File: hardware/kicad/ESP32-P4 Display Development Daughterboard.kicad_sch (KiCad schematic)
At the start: 0 parts

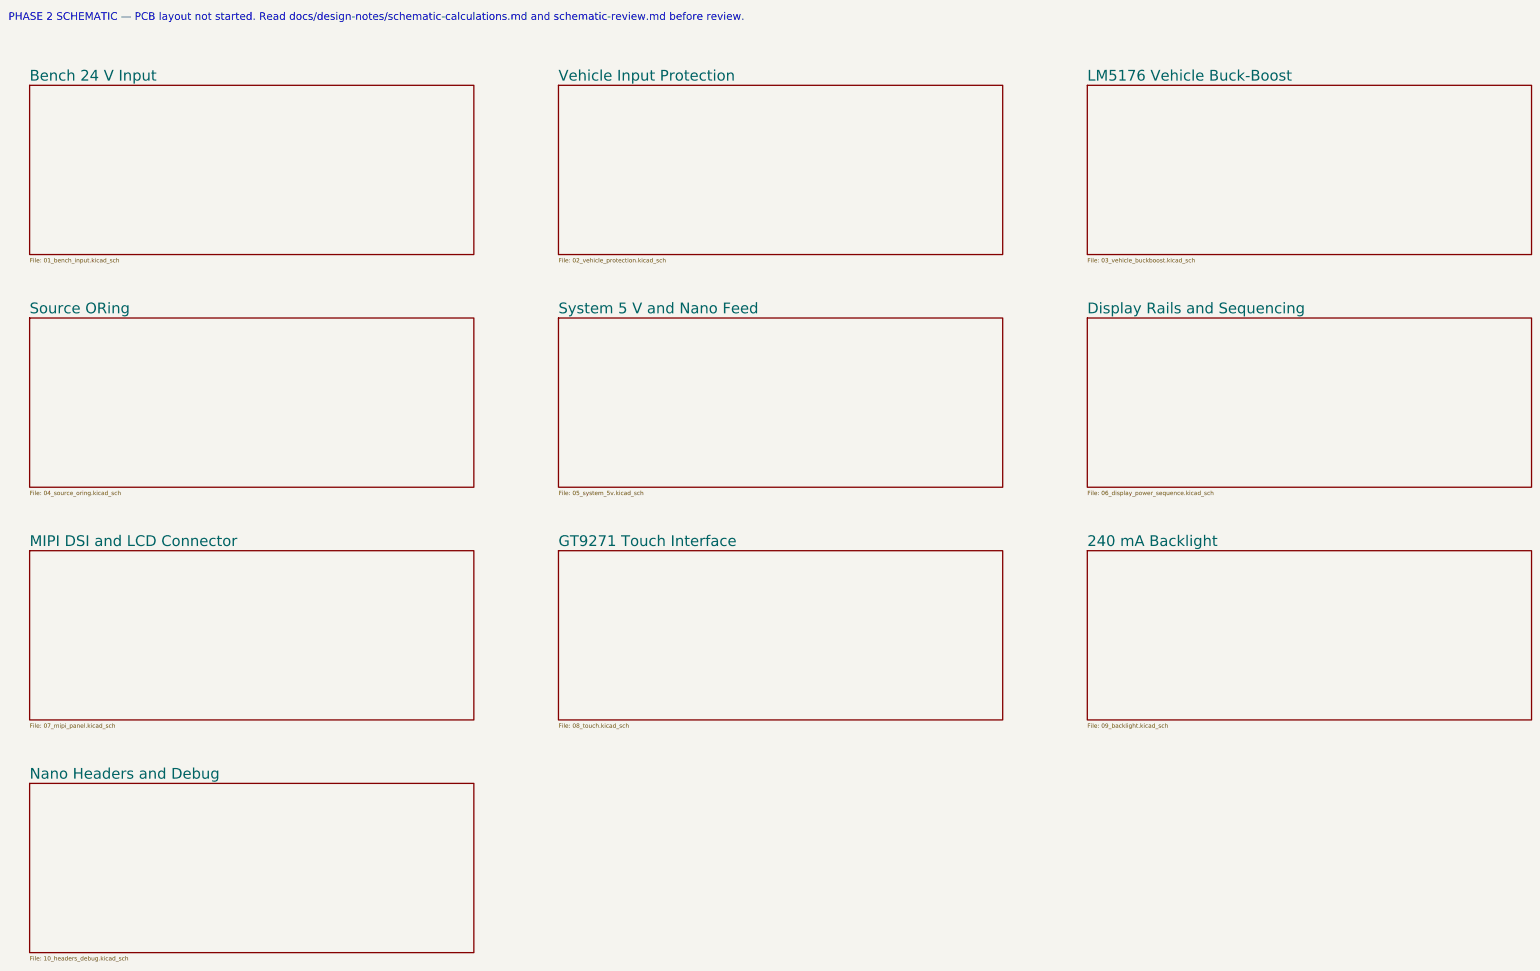
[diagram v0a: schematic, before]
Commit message: hardware: complete schematic maintainability and libraries
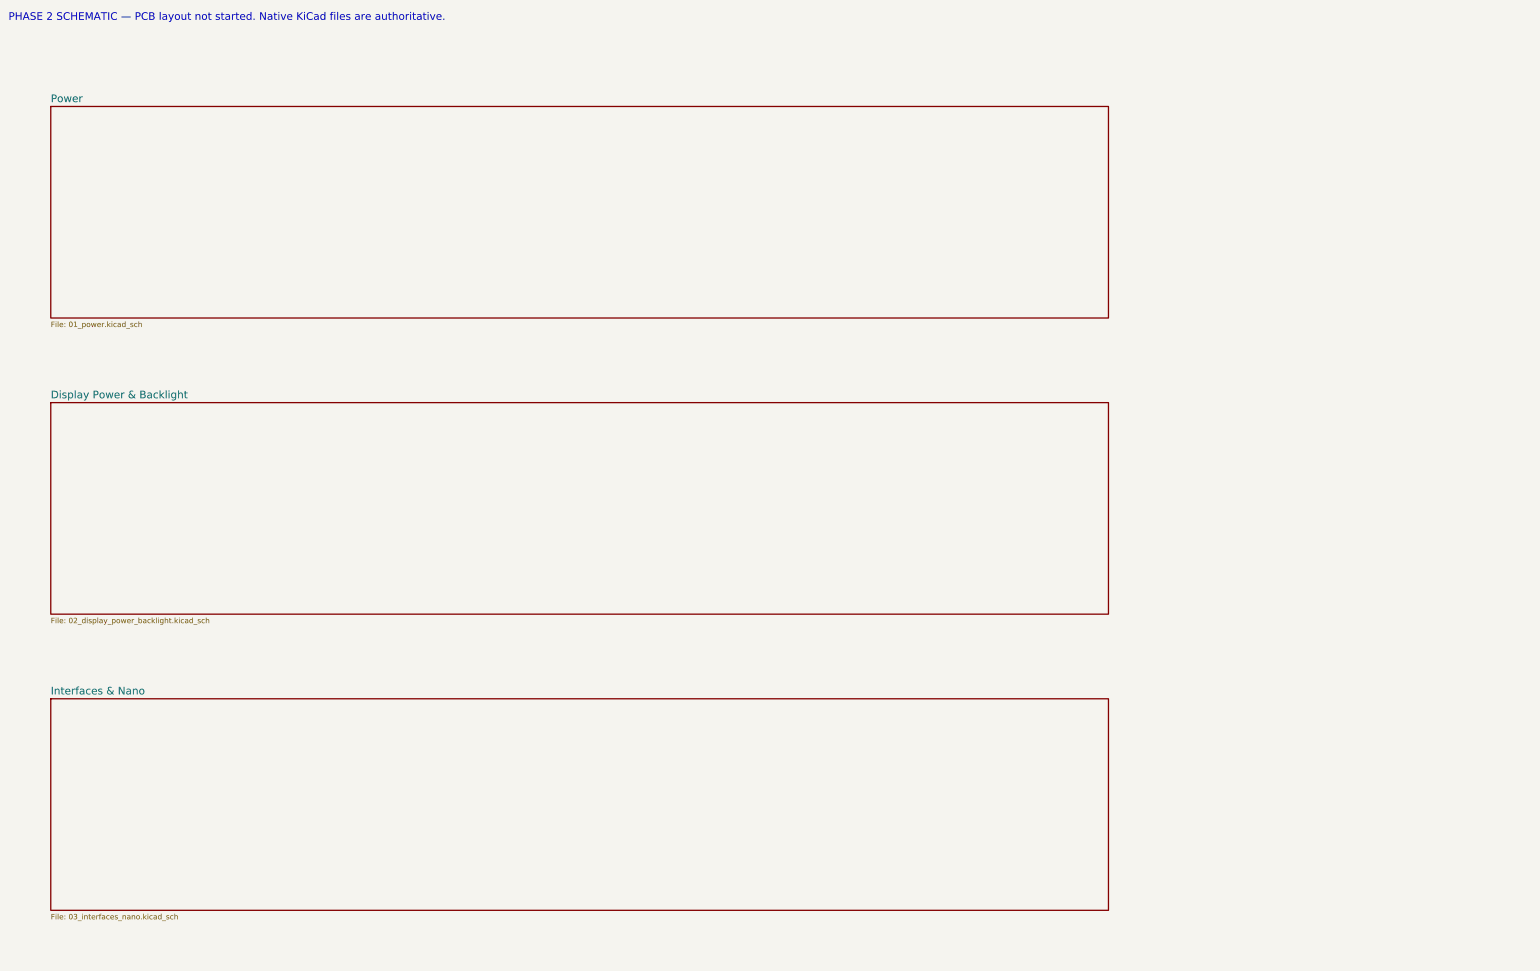
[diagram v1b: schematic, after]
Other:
- removed sheet 240 mA Backlight
- removed sheet Bench 24 V Input
- removed sheet Display Rails and Sequencing
- removed sheet GT9271 Touch Interface
- removed sheet LM5176 Vehicle Buck-Boost
- removed sheet MIPI DSI and LCD Connector
- removed sheet Nano Headers and Debug
- removed sheet Source ORing
- removed sheet System 5 V and Nano Feed
- removed sheet Vehicle Input Protection
- added sheet Display Power & Backlight (02_display_power_backlight.kicad_sch)
- added sheet Interfaces & Nano (03_interfaces_nano.kicad_sch)
- added sheet Power (01_power.kicad_sch)
- note added: "PHASE 2 SCHEMATIC — PCB layout not started. Native KiCad files are authoritative."
- note removed: "PHASE 2 SCHEMATIC — PCB layout not started. Read docs/design-notes/schematic-calculations.md and schematic-review.md before review."
